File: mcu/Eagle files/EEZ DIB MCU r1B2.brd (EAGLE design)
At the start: 139 x 70 mm, 193 parts, among them IC1 TPD4E001DRLR, IC10 TPS2051BDBVR, IC11 TPS61169DCKR, IC12 TPD4E001DRLR, IC13 TPA6205A1DGN, IC14 TPD4E001DRLR, IC15 AR1021-I/SS, IC16 TPD4E001DRLR, IC17 DP83848CVV/NOPB, IC2 SN74LVC2G34DBVR, IC3 BTS3408G, IC4 STM32F769IGT6, IC5 LD1117ADT33TR, IC6 TPD4E001DRLR, IC7 TPD4E001DRLR, IC8 IS42S16400J, IC9 BR24G64FVT-3AGE2, J1 5033981892, Q1 MMBT5551, SW1 PEC16-2215F-S0024, SW2 BSF-3152, X1 ZL263-40DG, X2 ZL231-16KG, X3 1844249, X4 ZL231-20KG, X5 292304-1, X6 LMJTAB881243M-L, Y1 10MHz

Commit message: #3
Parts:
- removed X5: 292304-1, EEZ_Lib1:USB-B
- added J2: 678038020, EEZ_Lib1:678038020
- moved IC12 6.66 mm to (77.0, 10.6)
- moved C49 6.60 mm to (79.4, 12.5)
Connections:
- net GND: now also J2.5
- net PE: now also J2.SH1, J2.SH1.1, J2.SH2, J2.SH2.2; no longer X5.M1, X5.M2
- net USB_D_N: now also J2.2; no longer X5.2
- net USB_D_P: now also IC12.2, J2.3; no longer IC12.4, X5.3
- net USB_OTG_FS_ID: now also IC12.4, J2.4; no longer X5.4
- net USB_OTG_FS_VBUS: now also J2.1; no longer X5.1
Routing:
- net USB_OTG_FS_VBUS: track 61.6 -> 79.5 mm, vias 2 -> 4
- net PE: track 158.7 -> 174.0 mm, vias 0 -> 1
- net USB_OTG_FS_ID: track 35.7 -> 42.2 mm, vias 3 -> 2
- net USB_D_N: track 29.1 -> 35.5 mm, vias 1 -> 0
- net SDMMC1_CK: track 72.5 -> 68.4 mm
- net SDMMC1_D0: track 59.3 -> 55.1 mm
- net SDMMC1_CMD: track 75.3 -> 71.2 mm
- net USB_D_P: track 32.2 -> 35.4 mm, vias 2 -> 0
- net GND: track 161.5 -> 161.8 mm, vias 154 -> 156
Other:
- board text added: "EEZ DIB MCU (09/2018 r1B2)"
- board text removed: "EEZ DIB MCU (08/2018 r1B1)"

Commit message: #4
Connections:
- net +3V3: no longer C45.1, L2.1, R28.1
- net +5V: now also C45.1, L2.1, R28.1
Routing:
- net +5V: track 170.6 -> 182.3 mm, vias 6 -> 7
- net +3V3: track 100.9 -> 93.3 mm, vias 73 -> 72
- net !RESET: track 213.0 -> 214.9 mm

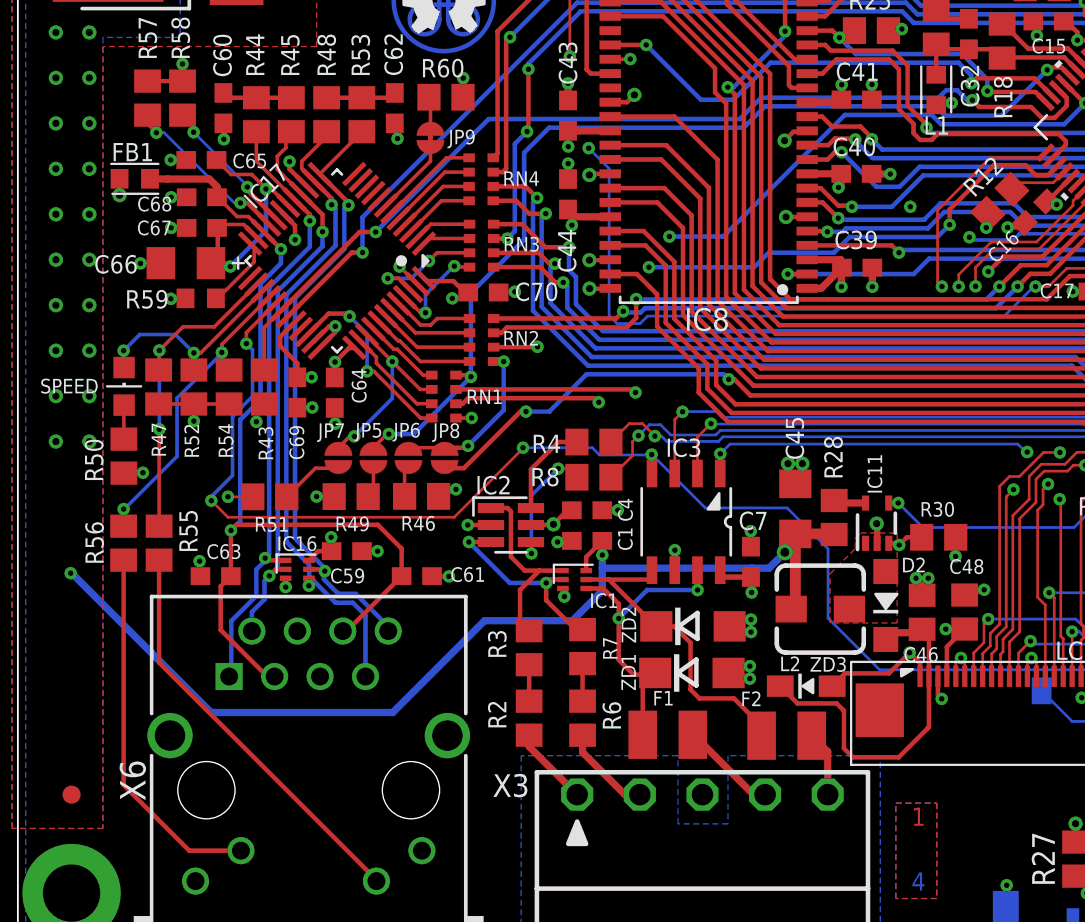
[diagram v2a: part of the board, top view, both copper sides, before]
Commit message: PCB parts images added
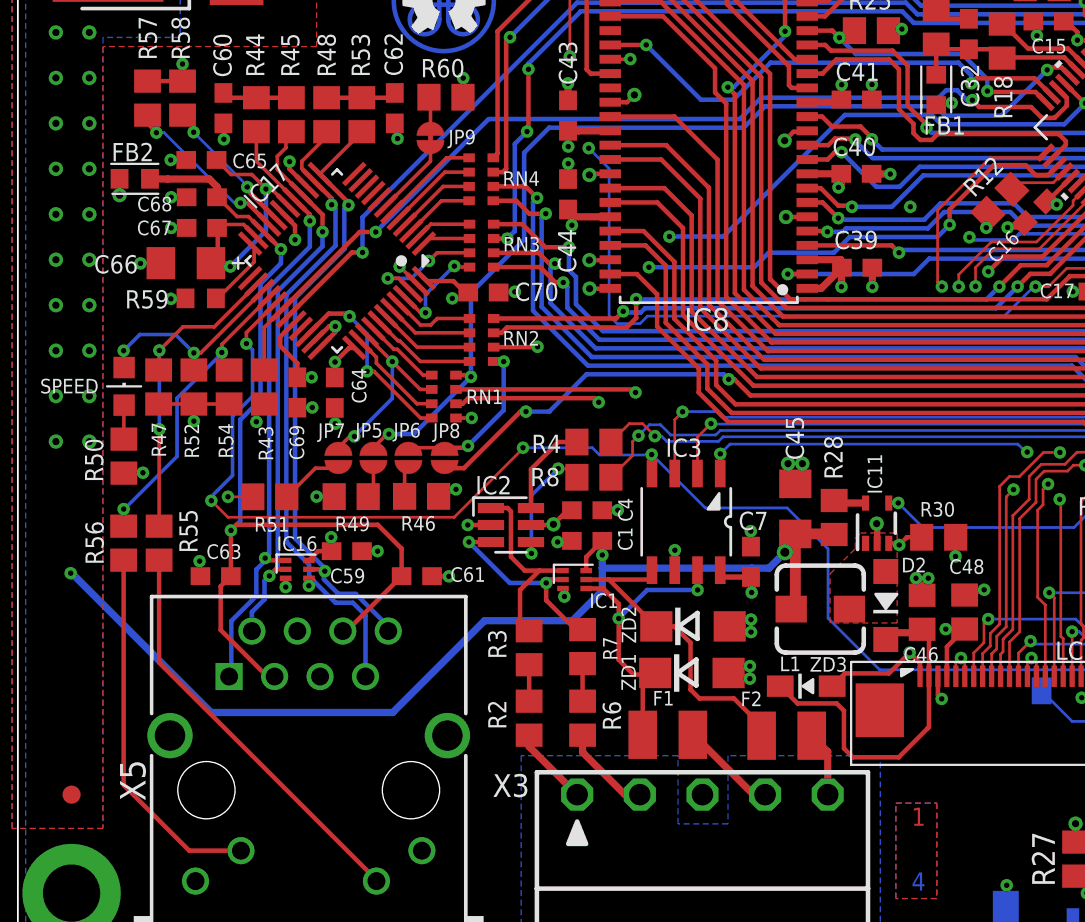
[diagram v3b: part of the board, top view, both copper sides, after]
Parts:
- removed L2: DLG-0403-4R7, EEZ_Lib1:DE0403
- added FB2: LCBA-600, EEZ_Lib1:BEAD0603
- C10: value 47u -> EEEFK1V470P
- C12: value 10u -> 4u7
- C47: value 4u7/16V (293D475X9016A2TE3) -> 4u7
- D2: value NSR0240 -> RB751V40T1G or NSR0240
- FB1: value 60R@100MHz -> LCBA-600
- J1: value 5033981892 -> 503398-1892
- J2: value 678038020 -> 67803-8020
- L1: value LCBA-600 -> DLG-0403-4R7; device EEZ_Lib1:BEAD0603 -> EEZ_Lib1:DE0403
- SW2: value BSF-3152 -> B3F-3152; device EEZ_switches:BSF-315X -> EEZ_switches:B3F-315X
- moved FB1 45.1 mm to (46.8, 48.4), turned to 90 degrees
- moved L1 29.7 mm to (40.3, 19.4)
- renumbered X6 to X5
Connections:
- net +3V3: now also FB2.P$1; no longer FB1.P$1
- net +3V3(A): now also FB2.P$2; no longer FB1.P$2
- net +5V: now also L1.1; no longer L2.1
- net SW_WLED: now also L1.2; no longer L2.2
- net VDD: now also FB1.P$1; no longer L1.P$1
- net VDDA: now also FB1.P$2; no longer L1.P$2

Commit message: minor changes in BOMs
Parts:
- C37: device rcl:C1210 -> rcl:C1206
- C56: value 220n -> 470n
- SPEED: value HSMY-C170 -> LTST-C170YKT
- moved R27 0.83 mm to (55.4, 5.40)
- moved C37 0.38 mm to (57.6, 5.91)

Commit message: SW2 changed
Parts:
- added TP1: (no value), EEZ_Lib1:PCB_SHIELD_TAB
- C37: value 10u -> 4u7
- D2: device EEZ_Lib1:SOD123 -> EEZ_Lib1:SOD323-R
- SW2: value B3F-3152 -> TL1100CF160Q; device EEZ_switches:B3F-315X -> EEZ_switches:TL1100C
- moved R27 7.88 mm to (63.3, 5.97), turned to 180 degrees
- moved JP4 6.84 mm to (71.3, 23.3)
- moved C3 5.52 mm to (126.9, 8.19), turned to 180 degrees
- moved C37 4.18 mm to (55.9, 2.08), turned to 180 degrees
- moved R26 3.79 mm to (63.3, 4.01), turned to 180 degrees
- moved ZD3 3.05 mm to (42.4, 13.9), turned to 90 degrees
- moved B1 2.28 mm to (121.9, 14.3)
- moved SW2 2.24 mm to (127.0, 4.00), turned to 90 degrees
- moved LCD1 1.52 mm to (57.2, 13.7)
- moved C55 0.76 mm to (68.8, 20.5)
- moved IC14 0.76 mm to (67.0, 18.6)
- moved RN2 0.48 mm to (21.9, 34.4)
- moved ZD2 0.33 mm to (33.1, 18.7)
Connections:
- net GND: now also TP1.1; no longer SW2.3, SW2.4
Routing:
- net N$24: track 7.02 -> 13.3 mm
- net VLED+: track 20.0 -> 16.2 mm
- net GND: track 161.6 -> 159.2 mm
- net LTDC_G7: track 56.5 -> 54.1 mm
- net N$4: track 29.1 -> 27.5 mm
- net LTDC_G3: track 58.5 -> 57.0 mm
- net LTDC_G5: track 57.9 -> 56.4 mm
- net LTDC_R7: track 43.9 -> 42.4 mm
- net N$70: track 26.7 -> 25.3 mm
- net SDMMC1_D0: track 55.1 -> 53.9 mm
- net N$50: track 10.3 -> 11.3 mm
- net SDMMC1_CK: track 68.4 -> 67.3 mm
- net +3V3: track 93.2 -> 94.1 mm, vias 72 -> 71
- net LTDC_R2: track 61.1 -> 60.3 mm
- net LTDC_HSYNC: track 46.0 -> 46.7 mm
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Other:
- board text added: "EEZ DIB MCU (10/2018 r1B2)"
- board text removed: "EEZ DIB MCU (09/2018 r1B2)"

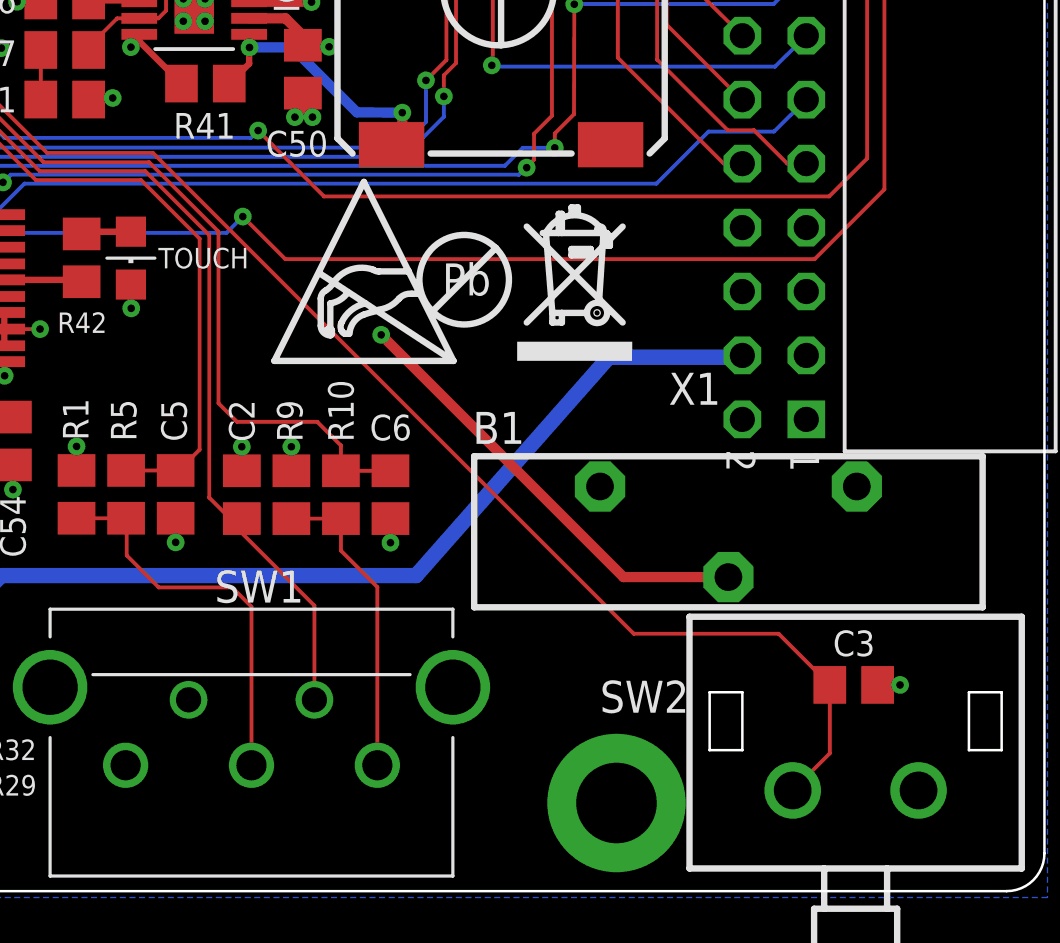
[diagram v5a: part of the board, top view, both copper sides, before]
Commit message: mcu board C3 relocated
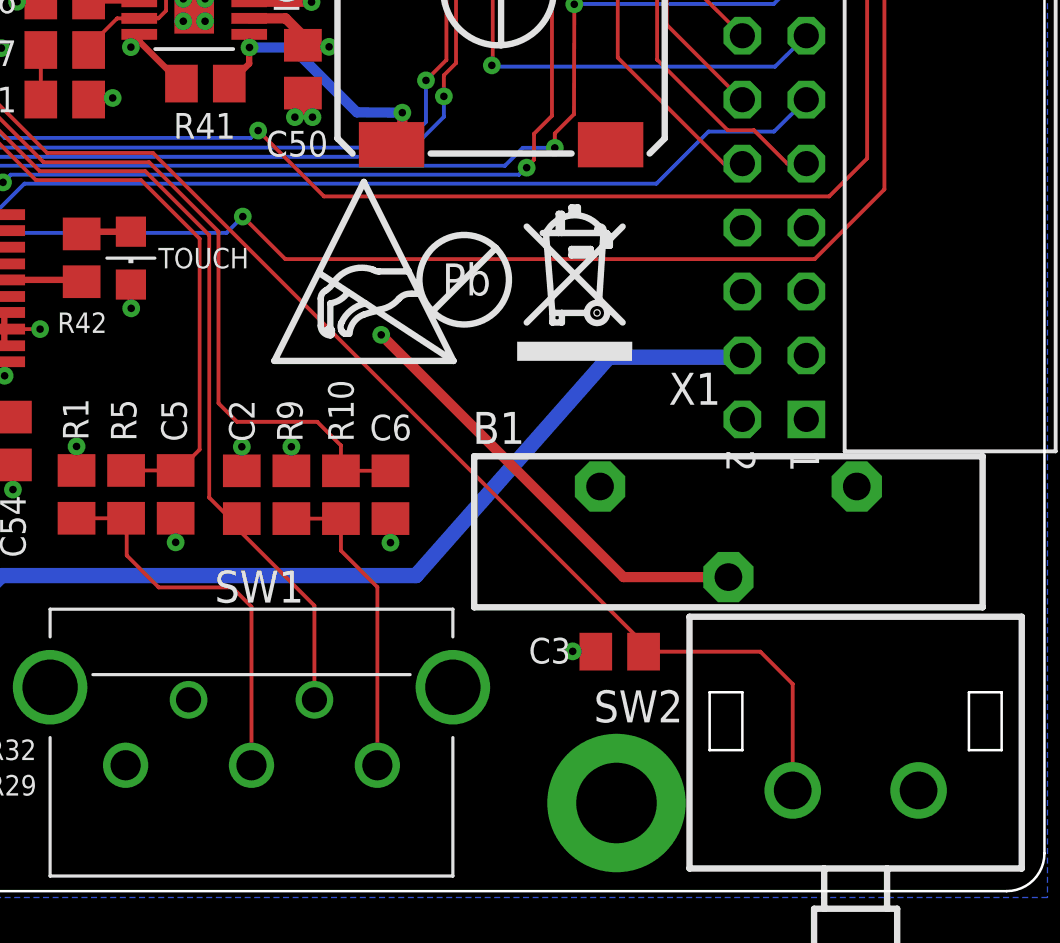
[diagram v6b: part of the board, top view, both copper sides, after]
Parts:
- moved C3 9.39 mm to (117.6, 9.51), turned to 0 degrees
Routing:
- net USER_SW: track 95.8 -> 94.0 mm
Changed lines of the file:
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@@
 <layer number="13" name="Route13" color="4" fill="5" visible="no" active="no"/>
 <layer number="14" name="Route14" color="1" fill="6" visible="no" active="no"/>
-<layer number="15" name="Power" color="6" fill="1" visible="yes" active="yes"/>
+<layer number="15" name="Power" color="6" fill="1" visible="no" active="yes"/>
 <layer number="16" name="Bottom" color="1" fill="1" visible="yes" active="yes"/>
 <layer number="17" name="Pads" color="6" fill="1" visible="yes" active="yes"/>
@@
 <attribute name="VALUE" x="81.0006" y="61.3537" size="1.016" layer="27" ratio="10"/>
 </element>
-<element name="C3" library="rcl" package="C0805" value="10n" x="126.9238" y="8.1915" smashed="yes" rot="R180">
-<attribute name="NAME" x="126.0983" y="9.3345" size="1.016" layer="25" ratio="10"/>
-<attribute name="VALUE" x="128.3208" y="8.6995" size="1.016" layer="27" ratio="10" rot="R180"/>
+<element name="C3" library="rcl" package="C0805" value="10n" x="117.6274" y="9.5123" smashed="yes">
+<attribute name="NAME" x="115.6843" y="10.0584" size="1.016" layer="25" ratio="10" rot="R180"/>
+<attribute name="VALUE" x="116.2304" y="9.0043" size="1.016" layer="27" ratio="10"/>
 </element>
 <element name="IC17" library="EEZ_Lib1" package="PT48" value="DP83848CVV/NOPB" x="13.335" y="38.8239" smashed="yes" rot="R225">
@@
 </element>
 <element name="SW2" library="EEZ_switches" package="TL1100C" value="TL1100CF160Q" x="127" y="4" smashed="yes" rot="R90">
-<attribute name="NAME" x="120.3833" y="8.3561" size="1.27" layer="25" ratio="10" rot="R180"/>
+<attribute name="NAME" x="120.142" y="7.9751" size="1.27" layer="25" ratio="10" rot="R180"/>
 <attribute name="VALUE" x="127.635" y="0.825" size="1.27" layer="27" ratio="10" rot="R90"/>
 </element>
@@
 <wire x1="99.9871" y1="14.8107" x2="99.9871" y2="13.8557" width="0.1524" layer="1"/>
 <wire x1="102.616" y1="17.653" x2="102.616" y2="16.698" width="0.1524" layer="1"/>
-<via x="128.7653" y="8.1915" extent="1-16" drill="0.3" shape="square"/>
+<via x="115.7605" y="9.525" extent="1-16" drill="0.3" shape="square"/>
 <via x="36.4109" y="19.0881" extent="1-16" drill="0.3" shape="square"/>
 <via x="26.035" y="20.066" extent="1-16" drill="0.3" shape="square"/>
@@
 <wire x1="70.0405" y1="23.4188" x2="69.9516" y2="23.2918" width="0.1524" layer="1"/>
 <contactref element="SW2" pad="2"/>
-<wire x1="128.7653" y1="8.1915" x2="127.8738" y2="8.1915" width="0.1524" layer="1"/>
+<wire x1="115.7605" y1="9.525" x2="116.6774" y2="9.5123" width="0.1524" layer="1"/>
 </signal>
 <signal name="+3V3">
@@
 <contactref element="IC4" pad="163"/>
 <contactref element="C3" pad="2"/>
-<wire x1="118.1862" y1="10.2235" x2="99.0854" y2="29.3243" width="0.1524" layer="1"/>
+<wire x1="118.5774" y1="9.8323" x2="99.0854" y2="29.3243" width="0.1524" layer="1"/>
 <wire x1="75.54290625" y1="58.3123125" x2="74.5236" y2="57.29300625" width="0.1524" layer="1"/>
 <wire x1="74.5236" y1="57.29300625" x2="74.5236" y2="55.7149" width="0.1524" layer="1"/>
@@
 <wire x1="94.8817" y1="29.3243" x2="92.3925" y2="31.8135" width="0.1524" layer="1"/>
 <contactref element="SW2" pad="1"/>
-<wire x1="123.9418" y1="10.2235" x2="118.1862" y2="10.2235" width="0.1524" layer="1"/>
-<wire x1="125.9738" y1="8.1915" x2="125.9738" y2="5.4738" width="0.1524" layer="1"/>
-<wire x1="125.9738" y1="5.4738" x2="124.5" y2="4" width="0.1524" layer="1"/>
-<wire x1="123.9418" y1="10.2235" x2="125.9738" y2="8.1915" width="0.1524" layer="1"/>
+<wire x1="118.5774" y1="9.5123" x2="123.2154" y2="9.5123" width="0.1524" layer="1"/>
+<wire x1="123.2154" y1="9.5123" x2="124.5" y2="8.2277" width="0.1524" layer="1"/>
+<wire x1="124.5" y1="4" x2="124.5" y2="8.2277" width="0.1524" layer="1"/>
+<wire x1="118.5774" y1="9.5123" x2="118.5774" y2="9.8323" width="0.1524" layer="1"/>
 </signal>
 <signal name="I2C1_SCL">

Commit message: #12
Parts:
- moved JP4 0.73 mm to (71.6, 23.9), turned to 90 degrees
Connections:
- net !RESET: now also JP4.NO; no longer JP4.NC
- net GND: now also JP4.NC; no longer JP4.NO
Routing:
- net !RESET: track 215.3 -> 214.1 mm
- net LTDC_G7: track 54.1 -> 55.0 mm
